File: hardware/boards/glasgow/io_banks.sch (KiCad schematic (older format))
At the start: 26 parts, among them J10 Conn_01x03, J4 Conn_01x02, J5 Conn_02x22_Odd_Even, U30 ICE40HX8K-BG121, U32 SN74LVC1T45DRL

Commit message: revC1: Updated part information and datasheet links
 - Added resistor network datasheet/part number
 - Updated blue, white, pink LED datasheet/part numbers
 - Updated capacitor datasheets/part numbers
 - Updated resistor part numbers
 - Added MPN/Mfg fields for
	* PCA6408APW
	* SN74LVC1T45DRL
	* ATECC508A
	* MG2040
	* ESD5Z5.0T1G
 - Added information for ferrite bead (600 ohm jellybean)
 - Fixed typo (MG2048 -> MG2040)
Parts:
- C33, C85: MPN TMK107BJ154KA-T -> TMK105BJ104KV-F
- D11: MPN (none) -> ESD5Z5.0T1G; Mfg (none) -> On Semiconductor
- D12, D13: Mfg (none) -> ON Semiconductor
- D6: MPN 150060GS75000 -> 150060BS75000
- D7: MPN 150060GS75000 -> OSK40603C1E; Mfg Wurth Electronics -> Optosupply
- D8: MPN 150060GS75000 -> SMLEN3WBC8W1; Mfg Wurth Electronics -> ROHM Semiconductor
- D9: MPN 150060YS75000 -> OSK40603C1E; Mfg Wurth Electronics -> Optosupply
- R10: MPN AC0603FR-07130RL -> RC0402FR-131KL
- R11: MPN RC0603FR-132K2L -> RC0402FR-134K7L
- R20: MPN RC0603FR-132K2L -> RC0402FR-1310KL
- R21: MPN RC0603FR-132K2L -> RC0402FR-136K8L
- R22: MPN RC0603FR-13390RL -> RC0402FR-1310KL
- R23: MPN RC0603FR-07604RL -> RC0402FR-134K7L
- R38, R39, R43: MPN AC0603FR-07130RL -> RC0402FR-1347RL
- R44: MPN AC0603FR-07130RL -> RC0402FR-1310KL
- R45: MPN AC0603FR-07130RL -> RC0402FR-1333RL
- U32: MPN (none) -> SN74LVC1T45DRL; Mfg (none) -> Texas Instruments

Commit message: revC1: add Vio active LEDs, misc fixes
- Move some vias that were gratuitously intruding into pads
- Update footprints that changed names upstream
- Beauty fixes
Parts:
- D10, D6, D7, D8, D9: footprint LED_SMD:LED_0603_1608Metric_Pad0.82x1.00mm_HandSolder -> LED_SMD:LED_0603_1608Metric_Pad1.05x0.95mm_HandSolder
- D12, D13: 1b2-bom-key esd-diode-sod523-esd5z5_0t1g -> (none); MPN (none) -> ESD5Z5.0T1G
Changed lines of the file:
@@
 F 0 "D6" H 9500 1050 50  0000 C CNN
 F 1 "BLU" H 9350 1050 50  0000 C CNN
-F 2 "LED_SMD:LED_0603_1608Metric_Pad0.82x1.00mm_HandSolder" H 9800 1050 50  0001 C CNN
+F 2 "LED_SMD:LED_0603_1608Metric_Pad1.05x0.95mm_HandSolder" H 9800 1050 50  0001 C CNN
 F 3 "https://www.mouser.com/datasheet/2/445/150060BS75000-368917.pdf" H 9800 1050 50  0001 C CNN
 F 4 "Wurth Electronics" H -450 150 50  0001 C CNN "Mfg"
@@
 F 0 "D7" H 9500 1250 50  0000 C CNN
 F 1 "PNK" H 9350 1250 50  0000 C CNN
-F 2 "LED_SMD:LED_0603_1608Metric_Pad0.82x1.00mm_HandSolder" H 9800 1250 50  0001 C CNN
+F 2 "LED_SMD:LED_0603_1608Metric_Pad1.05x0.95mm_HandSolder" H 9800 1250 50  0001 C CNN
 F 3 "https://lcsc.com/product-detail/Light-Emitting-Diodes-LED_OptoSupply-OSK40603C1E_C268294.html" H 9800 1250 50  0001 C CNN
 F 4 "Optosupply" H -450 150 50  0001 C CNN "Mfg"
@@
 F 0 "D8" H 9500 1450 50  0000 C CNN
 F 1 "WHT" H 9350 1450 50  0000 C CNN
-F 2 "LED_SMD:LED_0603_1608Metric_Pad0.82x1.00mm_HandSolder" H 9800 1450 50  0001 C CNN
+F 2 "LED_SMD:LED_0603_1608Metric_Pad1.05x0.95mm_HandSolder" H 9800 1450 50  0001 C CNN
 F 3 "https://www.mouser.com/datasheet/2/348/sml-e1-e-1139169.pdf" H 9800 1450 50  0001 C CNN
 F 4 "ROHM Semiconductor" H -450 150 50  0001 C CNN "Mfg"
@@
 F 0 "D9" H 9500 1650 50  0000 C CNN
 F 1 "PNK" H 9350 1650 50  0000 C CNN
-F 2 "LED_SMD:LED_0603_1608Metric_Pad0.82x1.00mm_HandSolder" H 9800 1650 50  0001 C CNN
+F 2 "LED_SMD:LED_0603_1608Metric_Pad1.05x0.95mm_HandSolder" H 9800 1650 50  0001 C CNN
 F 3 "https://lcsc.com/product-detail/Light-Emitting-Diodes-LED_OptoSupply-OSK40603C1E_C268294.html" H 9800 1650 50  0001 C CNN
 F 4 "Optosupply" H -450 150 50  0001 C CNN "Mfg"
@@
 F 0 "D10" H 9500 1850 50  0000 C CNN
 F 1 "BLU" H 9350 1850 50  0000 C CNN
-F 2 "LED_SMD:LED_0603_1608Metric_Pad0.82x1.00mm_HandSolder" H 9800 1850 50  0001 C CNN
+F 2 "LED_SMD:LED_0603_1608Metric_Pad1.05x0.95mm_HandSolder" H 9800 1850 50  0001 C CNN
 F 3 "https://www.mouser.com/datasheet/2/445/150060RS75000-368563.pdf" H 9800 1850 50  0001 C CNN
 F 4 "Wurth Electronics" H -450 150 50  0001 C CNN "Mfg"
@@
 F 3 "https://www.onsemi.com/pub/Collateral/ESD5Z2.5T1-D.PDF" H 2700 3350 50  0001 C CNN
 F 4 "ON Semiconductor" H 2700 3350 50  0001 C CNN "Mfg"
-F 5 "ESD5Z5.0T1G" H 2700 3350 50 0001 C CNN "MPN
-F 6 "esd-diode-sod523-esd5z5_0t1g" H 2700 3350 50  0001 C CNN "1b2-bom-key"
+F 5 "ESD5Z5.0T1G" H 2700 3350 50  0001 C CNN "MPN"
 	1    2700 3350
 	0    -1   -1   0
@@
 F 3 "https://www.onsemi.com/pub/Collateral/ESD5Z2.5T1-D.PDF" H 3000 3350 50  0001 C CNN
 F 4 "ON Semiconductor" H 3000 3350 50  0001 C CNN "Mfg"
-F 5 "ESD5Z5.0T1G" H 3000 3350 50 0001 C CNN "MPN
-F 6 "esd-diode-sod523-esd5z5_0t1g" H 3000 3350 50  0001 C CNN "1b2-bom-key"
+F 5 "ESD5Z5.0T1G" H 3000 3350 50  0001 C CNN "MPN"
 	1    3000 3350
 	0    -1   -1   0
@@
 Text Notes 3300 3350 0    50   ~ 0
 Auxiliary connector that \nmay be used for exper-\nimenting with addons. \nThere is no guarantee \nthat this connector will\nbe kept in future revisions.
+$Comp
+L Device:R R?
+U 1 1 5CB5DA66
+P 2050 2400
+AR Path="/5CB5DA66" Ref="R?"  Part="1"
+AR Path="/5C7B59B0/5CB5DA66" Ref="R45"  Part="1"
+F 0 "R45" V 1950 2400 50  0000 C CNN
+F 1 "33" V 2050 2450 50  0000 R CNN
+F 2 "Resistor_SMD:R_0402_1005Metric" V 1980 2400 50  0001 C CNN
+F 3 "https://www.mouser.com/datasheet/2/447/PYu-RC_Group_51_RoHS_L_10-1527934.pdf" H 2050 2400 50  0001 C CNN
+F 4 "Yageo" H -8300 -150 50  0001 C CNN "Mfg"
+F 5 "RC0402FR-1333RL" H -8300 -150 50  0001 C CNN "MPN"
+F 6 "res-0402-33" H 2050 2400 50  0001 C CNN "1b2-bom-key"
+	1    2050 2400
+	0    1    -1   0
+$EndComp
+Wire Wire Line
+	2200 2400 2250 2400
 Wire Bus Line
 	2400 4950 2400 5800
@@
 Wire Bus Line
 	9050 3200 9050 5800
-$Comp
-L Device:R R?
-U 1 1 5CB5DA66
-P 2050 2400
-AR Path="/5CB5DA66" Ref="R?"  Part="1"
-AR Path="/5C7B59B0/5CB5DA66" Ref="R45"  Part="1"
-F 0 "R45" V 1950 2400 50  0000 C CNN
-F 1 "33" V 2050 2450 50  0000 R CNN
-F 2 "Resistor_SMD:R_0402_1005Metric" V 1980 2400 50  0001 C CNN
-F 3 "https://www.mouser.com/datasheet/2/447/PYu-RC_Group_51_RoHS_L_10-1527934.pdf" H 2050 2400 50  0001 C CNN
-F 4 "Yageo" H -8300 -150 50  0001 C CNN "Mfg"
-F 5 "RC0402FR-1333RL" H -8300 -150 50  0001 C CNN "MPN"
-F 6 "res-0402-33" H 2050 2400 50  0001 C CNN "1b2-bom-key"
-	1    2050 2400
-	0    1    -1   0
-$EndComp
-Wire Wire Line
-	2200 2400 2250 2400
 $EndSCHEMATC

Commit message: revC1: clean up some datasheet links & MPNs
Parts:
- D10: MPN 150060RS75000 -> 150060BS75000
- D12, D13: 1b2-bom-key (none) -> esd-diode-sod523-esd5z5_0t1g
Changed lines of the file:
@@
 F 1 "BLU" H 9350 1850 50  0000 C CNN
 F 2 "LED_SMD:LED_0603_1608Metric_Pad1.05x0.95mm_HandSolder" H 9800 1850 50  0001 C CNN
-F 3 "https://www.mouser.com/datasheet/2/445/150060RS75000-368563.pdf" H 9800 1850 50  0001 C CNN
+F 3 "https://www.mouser.com/datasheet/2/445/150060BS75000-368917.pdf" H 9800 1850 50  0001 C CNN
 F 4 "Wurth Electronics" H -450 150 50  0001 C CNN "Mfg"
-F 5 "150060RS75000" H -450 150 50  0001 C CNN "MPN"
+F 5 "150060BS75000" H -450 150 50  0001 C CNN "MPN"
 F 6 "led-0603-blu" H 9800 1850 50  0001 C CNN "1b2-bom-key"
 	1    9800 1850
@@
 F 1 "4k7" V 9450 1050 50  0000 C CNN
 F 2 "Resistor_SMD:R_0402_1005Metric" V 9380 1050 50  0001 C CNN
-F 3 "https://www.mouser.com/datasheet/2/447/PYu-RC_Group_51_RoHS_L_9-1314892.pdf" H 9450 1050 50  0001 C CNN
+F 3 "https://www.mouser.com/datasheet/2/447/PYu-RC_Group_51_RoHS_L_10-1527934.pdf" H 9450 1050 50  0001 C CNN
 F 4 "Yageo" H -450 150 50  0001 C CNN "Mfg"
 F 5 "RC0402FR-134K7L" H -450 150 50  0001 C CNN "MPN"
@@
 F 1 "10k" V 9450 1650 50  0000 C CNN
 F 2 "Resistor_SMD:R_0402_1005Metric" V 9380 1650 50  0001 C CNN
-F 3 "https://www.mouser.com/datasheet/2/447/PYu-RC_Group_51_RoHS_L_9-1314892.pdf" H 9450 1650 50  0001 C CNN
+F 3 "https://www.mouser.com/datasheet/2/447/PYu-RC_Group_51_RoHS_L_10-1527934.pdf" H 9450 1650 50  0001 C CNN
 F 4 "Yageo" H -450 150 50  0001 C CNN "Mfg"
 F 5 "RC0402FR-1310KL" H -450 150 50  0001 C CNN "MPN"
@@
 F 1 "4k7" V 9450 1850 50  0000 C CNN
 F 2 "Resistor_SMD:R_0402_1005Metric" V 9380 1850 50  0001 C CNN
-F 3 "https://www.mouser.hk/datasheet/2/447/PYu-RC_Group_51_RoHS_L_9-1314892.pdf" H 9450 1850 50  0001 C CNN
+F 3 "https://www.mouser.com/datasheet/2/447/PYu-RC_Group_51_RoHS_L_10-1527934.pdf" H 9450 1850 50  0001 C CNN
 F 4 "Yageo" H -450 150 50  0001 C CNN "Mfg"
 F 5 "RC0402FR-134K7L" H -450 150 50  0001 C CNN "MPN"
@@
 F 1 "10k" V 9450 1250 50  0000 C CNN
 F 2 "Resistor_SMD:R_0402_1005Metric" V 9380 1250 50  0001 C CNN
-F 3 "https://www.mouser.com/datasheet/2/447/PYu-RC_Group_51_RoHS_L_9-1314892.pdf" H 9450 1250 50  0001 C CNN
+F 3 "https://www.mouser.com/datasheet/2/447/PYu-RC_Group_51_RoHS_L_10-1527934.pdf" H 9450 1250 50  0001 C CNN
 F 4 "Yageo" H -450 150 50  0001 C CNN "Mfg"
 F 5 "RC0402FR-1310KL" H -450 150 50  0001 C CNN "MPN"
@@
 F 1 "6k8" V 9450 1450 50  0000 C CNN
 F 2 "Resistor_SMD:R_0402_1005Metric" V 9380 1450 50  0001 C CNN
-F 3 "https://www.mouser.com/datasheet/2/447/PYu-RC_Group_51_RoHS_L_9-1314892.pdf" H 9450 1450 50  0001 C CNN
+F 3 "https://www.mouser.com/datasheet/2/447/PYu-RC_Group_51_RoHS_L_10-1527934.pdf" H 9450 1450 50  0001 C CNN
 F 4 "Yageo" H -450 150 50  0001 C CNN "Mfg"
 F 5 "RC0402FR-136K8L" H -450 150 50  0001 C CNN "MPN"
@@
 F 1 "u1" H 8965 2605 50  0000 L CNN
 F 2 "Capacitor_SMD:C_0402_1005Metric" H 8888 2500 50  0001 C CNN
-F 3 "https://www.mouser.hk/datasheet/2/396/mlcc02_e-1307760.pdf" H 8850 2650 50  0001 C CNN
+F 3 "https://www.mouser.com/datasheet/2/396/mlcc02_e-1307760.pdf" H 8850 2650 50  0001 C CNN
 F 4 "Taiyo Yuden" H 2200 1250 50  0001 C CNN "Mfg"
 F 5 "TMK105BJ104KV-F" H 2200 1250 50  0001 C CNN "MPN"
@@
 F 1 "u1" H 2215 1855 50  0000 L CNN
 F 2 "Capacitor_SMD:C_0402_1005Metric" H 2138 1750 50  0001 C CNN
-F 3 "https://www.mouser.hk/datasheet/2/396/mlcc02_e-1307760.pdf" H 2100 1900 50  0001 C CNN
+F 3 "https://www.mouser.com/datasheet/2/396/mlcc02_e-1307760.pdf" H 2100 1900 50  0001 C CNN
 F 4 "Taiyo Yuden" H -4550 500 50  0001 C CNN "Mfg"
 F 5 "TMK105BJ104KV-F" H -4550 500 50  0001 C CNN "MPN"
@@
 F 4 "ON Semiconductor" H 2700 3350 50  0001 C CNN "Mfg"
 F 5 "ESD5Z5.0T1G" H 2700 3350 50  0001 C CNN "MPN"
+F 6 "esd-diode-sod523-esd5z5_0t1g" H 0   0   50  0001 C CNN "1b2-bom-key"
 	1    2700 3350
 	0    -1   -1   0
@@
 F 4 "ON Semiconductor" H 3000 3350 50  0001 C CNN "Mfg"
 F 5 "ESD5Z5.0T1G" H 3000 3350 50  0001 C CNN "MPN"
+F 6 "esd-diode-sod523-esd5z5_0t1g" V 3000 3350 50  0001 C CNN "1b2-bom-key"
 	1    3000 3350
 	0    -1   -1   0

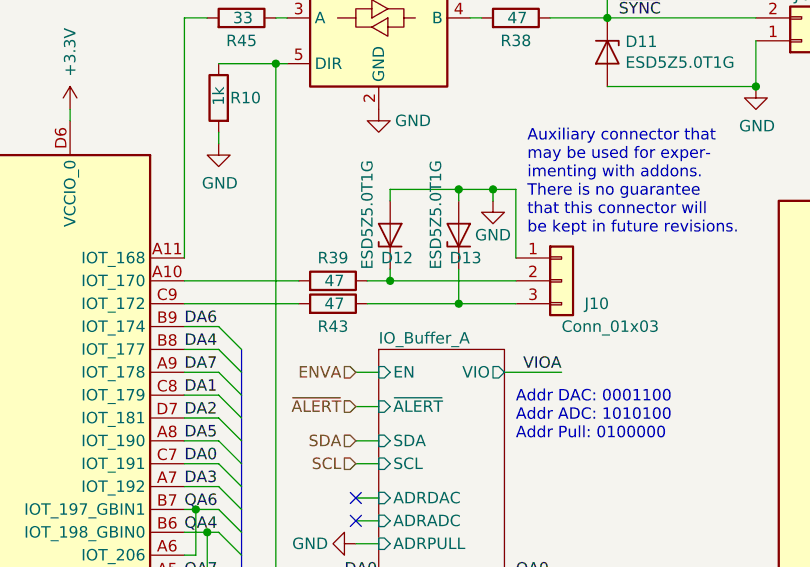
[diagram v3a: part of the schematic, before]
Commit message: revC1: remove DNP part models & add DNP field in sch
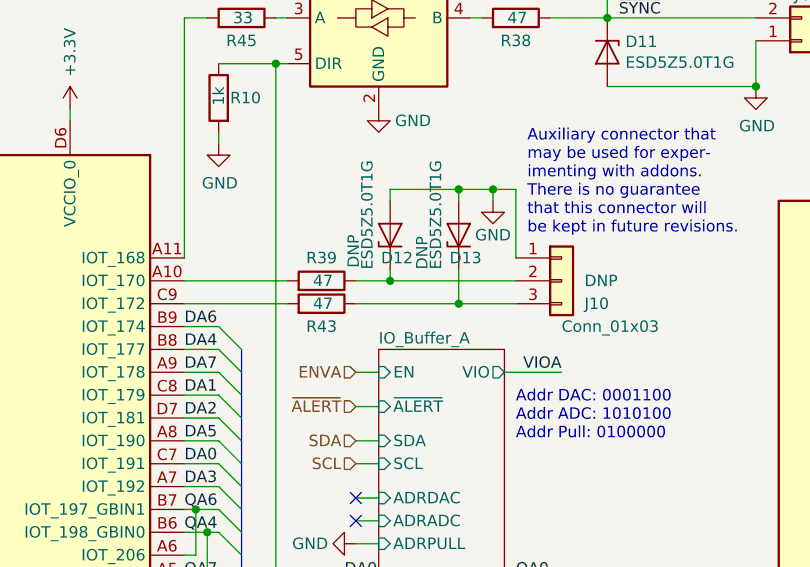
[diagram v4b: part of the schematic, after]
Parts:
- D12, D13, J10: DNP (none) -> DNP
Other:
- moved on the sheet: R39, R43
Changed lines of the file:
@@
 F 3 "~" H 3450 3550 50  0001 C CNN
 F 4 "conn-th-01in-3-1-hdr" H 3450 3550 50  0001 C CNN "1b2-bom-key"
+F 5 "DNP" H 3550 3550 50  0000 L CNN "DNP"
 	1    3450 3550
 	1    0    0    -1
@@
 	3050 2400 3100 2400
 Wire Wire Line
-	1800 3550 2300 3550
-Wire Wire Line
-	1800 3650 2300 3650
+	1800 3550 2250 3550
+Wire Wire Line
+	1800 3650 2250 3650
 Wire Wire Line
 	2250 2600 2200 2600
@@
 Wire Wire Line
 	3400 2400 3650 2400
-$Comp
-L Device:R R?
-U 1 1 5CBF658E
-P 2450 3550
-AR Path="/5CBF658E" Ref="R?"  Part="1"
-AR Path="/5C7B59B0/5CBF658E" Ref="R39"  Part="1"
-F 0 "R39" V 2550 3550 50  0000 C CNN
-F 1 "47" V 2450 3600 50  0000 R CNN
-F 2 "Resistor_SMD:R_0402_1005Metric" V 2380 3550 50  0001 C CNN
-F 3 "https://www.mouser.com/datasheet/2/447/PYu-RC_Group_51_RoHS_L_10-1527934.pdf" H 2450 3550 50  0001 C CNN
-F 4 "Yageo" H -7900 1000 50  0001 C CNN "Mfg"
-F 5 "RC0402FR-1347RL" H -7900 1000 50  0001 C CNN "MPN"
-F 6 "res-0402-47" H 2450 3550 50  0001 C CNN "1b2-bom-key"
-	1    2450 3550
-	0    1    -1   0
-$EndComp
-$Comp
-L Device:R R?
-U 1 1 5CBF65F8
-P 2450 3650
-AR Path="/5CBF65F8" Ref="R?"  Part="1"
-AR Path="/5C7B59B0/5CBF65F8" Ref="R43"  Part="1"
-F 0 "R43" V 2350 3650 50  0000 C CNN
-F 1 "47" V 2450 3700 50  0000 R CNN
-F 2 "Resistor_SMD:R_0402_1005Metric" V 2380 3650 50  0001 C CNN
-F 3 "https://www.mouser.com/datasheet/2/447/PYu-RC_Group_51_RoHS_L_10-1527934.pdf" H 2450 3650 50  0001 C CNN
-F 4 "Yageo" H -7900 1100 50  0001 C CNN "Mfg"
-F 5 "RC0402FR-1347RL" H -7900 1100 50  0001 C CNN "MPN"
-F 6 "res-0402-47" H 2450 3650 50  0001 C CNN "1b2-bom-key"
-	1    2450 3650
-	0    1    -1   0
-$EndComp
-Wire Wire Line
-	2600 3650 3000 3650
-Wire Wire Line
-	2600 3550 2700 3550
+Wire Wire Line
+	2550 3650 3000 3650
+Wire Wire Line
+	2550 3550 2700 3550
 $Comp
 L power:PWR_FLAG #FLG0101
@@
 F 5 "ESD5Z5.0T1G" H 2700 3350 50  0001 C CNN "MPN"
 F 6 "esd-diode-sod523-esd5z5_0t1g" H 0   0   50  0001 C CNN "1b2-bom-key"
+F 7 "DNP" H 2630 3510 50  0000 C CNN "DNP"
 	1    2700 3350
 	0    -1   -1   0
@@
 F 5 "ESD5Z5.0T1G" H 3000 3350 50  0001 C CNN "MPN"
 F 6 "esd-diode-sod523-esd5z5_0t1g" V 3000 3350 50  0001 C CNN "1b2-bom-key"
+F 7 "DNP" H 2850 3510 50  0000 L CNN "DNP"
 	1    3000 3350
 	0    -1   -1   0
@@
 Wire Wire Line
 	2200 2400 2250 2400
+$Comp
+L Device:R R?
+U 1 1 5CBF65F8
+P 2400 3650
+AR Path="/5CBF65F8" Ref="R?"  Part="1"
+AR Path="/5C7B59B0/5CBF65F8" Ref="R43"  Part="1"
+F 0 "R43" V 2300 3650 50  0000 C CNN
+F 1 "47" V 2400 3700 50  0000 R CNN
+F 2 "Resistor_SMD:R_0402_1005Metric" V 2330 3650 50  0001 C CNN
+F 3 "https://www.mouser.com/datasheet/2/447/PYu-RC_Group_51_RoHS_L_10-1527934.pdf" H 2400 3650 50  0001 C CNN
+F 4 "Yageo" H -7950 1100 50  0001 C CNN "Mfg"
+F 5 "RC0402FR-1347RL" H -7950 1100 50  0001 C CNN "MPN"
+F 6 "res-0402-47" H 2400 3650 50  0001 C CNN "1b2-bom-key"
+	1    2400 3650
+	0    1    -1   0
+$EndComp
+$Comp
+L Device:R R?
+U 1 1 5CBF658E
+P 2400 3550
+AR Path="/5CBF658E" Ref="R?"  Part="1"
+AR Path="/5C7B59B0/5CBF658E" Ref="R39"  Part="1"
+F 0 "R39" V 2500 3550 50  0000 C CNN
+F 1 "47" V 2400 3600 50  0000 R CNN
+F 2 "Resistor_SMD:R_0402_1005Metric" V 2330 3550 50  0001 C CNN
+F 3 "https://www.mouser.com/datasheet/2/447/PYu-RC_Group_51_RoHS_L_10-1527934.pdf" H 2400 3550 50  0001 C CNN
+F 4 "Yageo" H -7950 1000 50  0001 C CNN "Mfg"
+F 5 "RC0402FR-1347RL" H -7950 1000 50  0001 C CNN "MPN"
+F 6 "res-0402-47" H 2400 3550 50  0001 C CNN "1b2-bom-key"
+	1    2400 3550
+	0    1    -1   0
+$EndComp
 Wire Bus Line
 	2400 4950 2400 5800

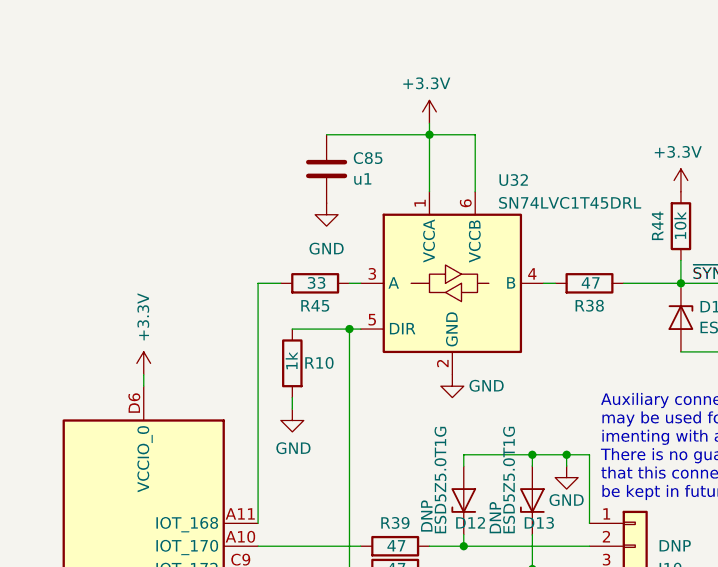
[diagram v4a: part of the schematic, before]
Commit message: revC1: reduce count of different resistor values
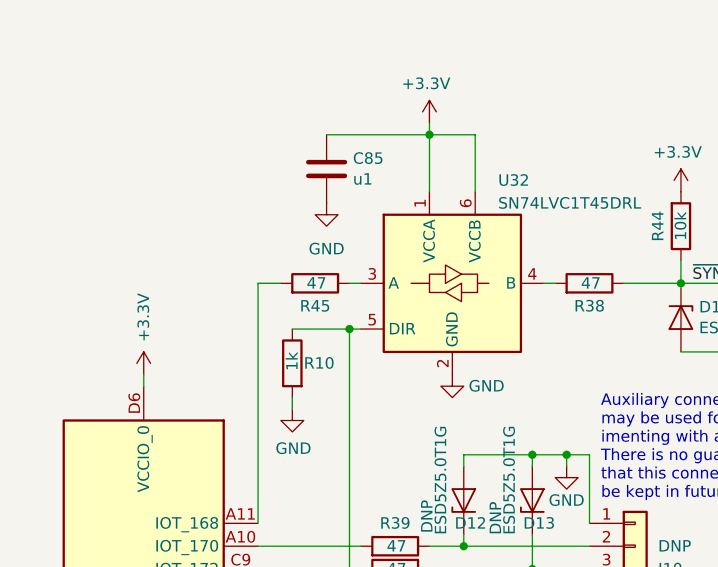
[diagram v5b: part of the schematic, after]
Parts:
- R45: value 33 -> 47; 1b2-bom-key res-0402-33 -> res-0402-47; MPN RC0402FR-1333RL -> RC0402FR-1347RL
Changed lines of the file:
@@
 AR Path="/5C7B59B0/5CB5DA66" Ref="R45"  Part="1"
 F 0 "R45" V 1950 2400 50  0000 C CNN
-F 1 "33" V 2050 2450 50  0000 R CNN
+F 1 "47" V 2050 2450 50  0000 R CNN
 F 2 "Resistor_SMD:R_0402_1005Metric" V 1980 2400 50  0001 C CNN
 F 3 "https://www.mouser.com/datasheet/2/447/PYu-RC_Group_51_RoHS_L_10-1527934.pdf" H 2050 2400 50  0001 C CNN
 F 4 "Yageo" H -8300 -150 50  0001 C CNN "Mfg"
-F 5 "RC0402FR-1333RL" H -8300 -150 50  0001 C CNN "MPN"
-F 6 "res-0402-33" H 2050 2400 50  0001 C CNN "1b2-bom-key"
+F 5 "RC0402FR-1347RL" H -8300 -150 50  0001 C CNN "MPN"
+F 6 "res-0402-47" H 2050 2400 50  0001 C CNN "1b2-bom-key"
 	1    2050 2400
 	0    1    -1   0

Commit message: revC1: replace Sync connector with proper Molex KK footprint
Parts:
- J4: footprint Connector_PinHeader_2.54mm:PinHeader_1x02_P2.54mm_Horizontal -> Glasgow:Molex_KK-254_1x02_P2.54mm_Horizontal
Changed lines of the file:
@@
 F 0 "J4" H 4500 2300 50  0000 C CNN
 F 1 "Conn_01x02" H 4580 2401 50  0001 L CNN
-F 2 "Connector_PinHeader_2.54mm:PinHeader_1x02_P2.54mm_Horizontal" H 4500 2500 50  0001 C CNN
+F 2 "Glasgow:Molex_KK-254_1x02_P2.54mm_Horizontal" H 4500 2500 50  0001 C CNN
 F 3 "https://www.mouser.hk/datasheet/2/418/NG_CD_640455_Y3-1255934.pdf" H 4500 2500 50  0001 C CNN
 F 4 "Molex" H -6100 -350 50  0001 C CNN "Mfg"

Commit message: RevC1: Added missing component MPN/Mfg values
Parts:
- J5: MPN (none) -> FTS-122-01-L-DV; Mfg (none) -> Samtec Inc.
- U30: MPN (none) -> ICE40HX8K-BG121; Mfg (none) -> Lattice Semiconductor Corporation
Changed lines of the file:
@@
 F 3 "http://www.latticesemi.com/Products/FPGAandCPLD/iCE40" H 3900 5450 50  0001 C CNN
 F 4 "ic-ice40hx8k-bg121" H 4750 4450 50  0001 C CNN "1b2-bom-key"
+F 5 "ICE40HX8K-BG121" H 4750 4450 50  0001 C CNN "MPN"
+F 6 "Lattice Semiconductor Corporation" H 4750 4450 50  0001 C CNN "Mfg"
 	2    4750 4450
 	-1   0    0    -1
@@
 F 3 "http://www.latticesemi.com/Products/FPGAandCPLD/iCE40" H 7400 5200 50  0001 C CNN
 F 4 "ic-ice40hx8k-bg121" H 8250 4200 50  0001 C CNN "1b2-bom-key"
+F 5 "ICE40HX8K-BG121" H 8250 4200 50  0001 C CNN "MPN"
+F 6 "Lattice Semiconductor Corporation" H 8250 4200 50  0001 C CNN "Mfg"
 	4    8250 4200
 	-1   0    0    -1
@@
 F 3 "~" H 10000 4300 50  0001 C CNN
 F 4 "conn-smd-005in-22-2-hdr" H 10000 4300 50  0001 C CNN "1b2-bom-key"
+F 5 "FTS-122-01-L-DV" H 10000 4300 50  0001 C CNN "MPN"
+F 6 "Samtec Inc." H 10000 4300 50  0001 C CNN "Mfg"
 	1    10000 4300
 	1    0    0    -1
@@
 F 3 "http://www.latticesemi.com/Products/FPGAandCPLD/iCE40" H 450 5250 50  0001 C CNN
 F 4 "ic-ice40hx8k-bg121" H 1300 4250 50  0001 C CNN "1b2-bom-key"
+F 5 "ICE40HX8K-BG121" H 1300 4250 50  0001 C CNN "MPN"
+F 6 "Lattice Semiconductor Corporation" H 1300 4250 50  0001 C CNN "Mfg"
 	1    1300 4250
 	-1   0    0    -1
